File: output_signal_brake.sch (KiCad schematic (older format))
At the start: 35 parts

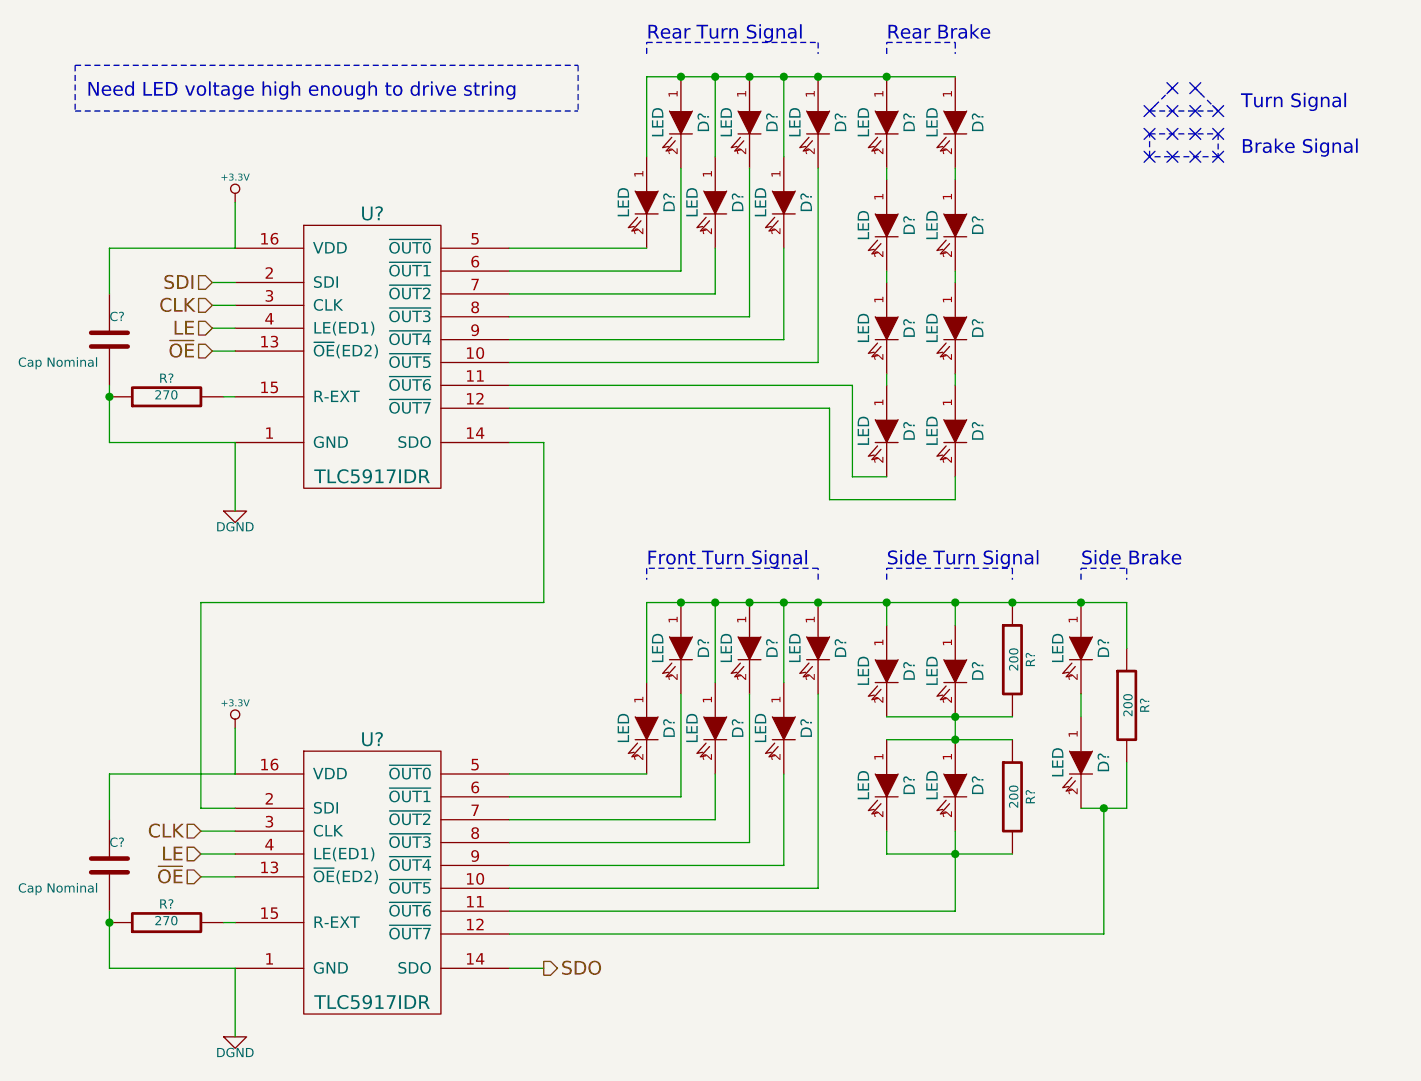
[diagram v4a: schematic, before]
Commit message: revised LED parts to match reality
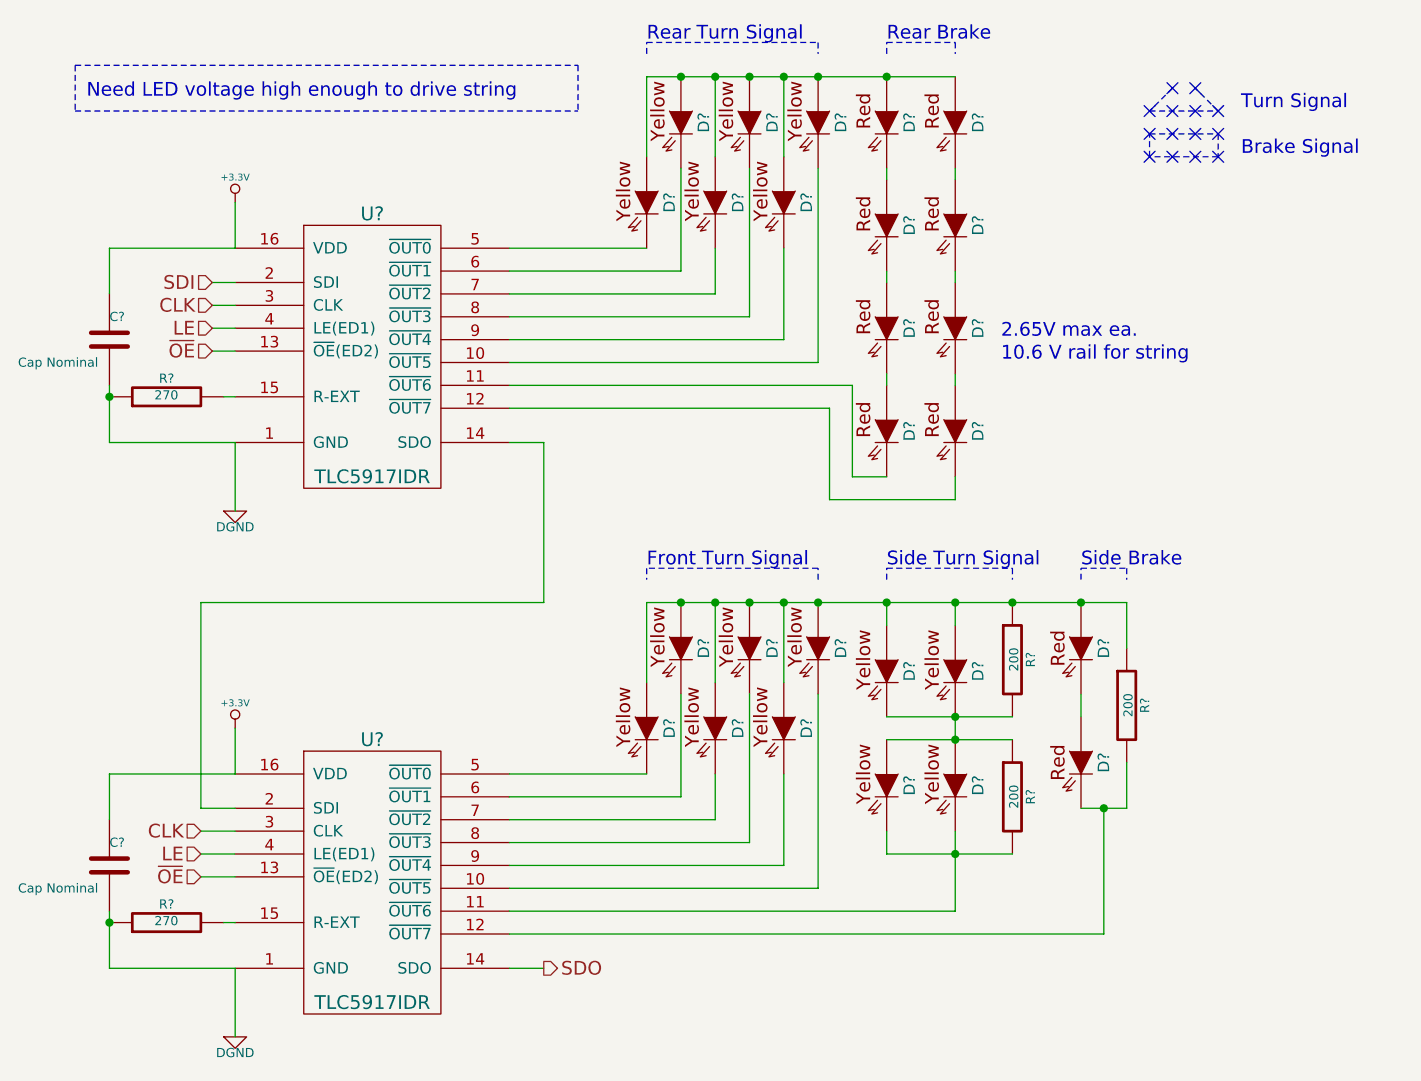
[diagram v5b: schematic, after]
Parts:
- removed D? (x26): LED, ~, symbol LED
- added D? (x8): LS-E63F, ~, symbol LS-E63F
- added D? (x6): LY-E63F, ~, symbol LY-E63F
- added D? (x2): LR-A67F, ~, symbol LR-A67F
- added D? (x10): LY-A67F, ~, symbol LY-A67F
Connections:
- net at U?.10 (~OUT5): now also D?.4 (Cathode)
- net at U?.11 (~OUT6): now also D?.4 (Cathode)
- net at U?.12 (~OUT7): now also D?.4 (Cathode)
- net at U?.5 (~OUT0): now also D?.4 (Cathode)
- net at U?.6 (~OUT1): now also D?.4 (Cathode)
- net at U?.7 (~OUT2): now also D?.4 (Cathode)
- net at U?.8 (~OUT3): now also D?.4 (Cathode)
- net at U?.9 (~OUT4): now also D?.4 (Cathode)
- net at U?.10 (~OUT5): now also D?.2 (Cathode)
- net at R?.2, U?.11 (~OUT6): now also D?.2 (Cathode), D?.2 (Cathode)
- net at R?.2, U?.12 (~OUT7): now also D?.2 (Cathode)
- net at U?.5 (~OUT0): now also D?.2 (Cathode)
- net at U?.6 (~OUT1): now also D?.2 (Cathode)
- net at U?.7 (~OUT2): now also D?.2 (Cathode)
- net at U?.8 (~OUT3): now also D?.2 (Cathode)
- net at U?.9 (~OUT4): now also D?.2 (Cathode)
- net at R?.1, R?.1: now also D?.1 (Anode), D?.1 (Anode), D?.1 (Anode), D?.1 (Anode), D?.1 (Anode), D?.1 (Anode), D?.1 (Anode), D?.1 (Anode), D?.1 (Anode)
- net at R?.1, R?.2: now also D?.1 (Anode), D?.1 (Anode), D?.2 (Cathode), D?.2 (Cathode)
- new net: D?.1 (Anode), D?.1 (Anode), D?.1 (Anode), D?.1 (Anode), D?.1 (Anode), D?.1 (Anode), D?.1 (Anode), D?.1 (Anode)
- new net: D?.1 (Anode), D?.4 (Cathode) (x6)
- new net: D?.1 (Anode), D?.2 (Cathode)
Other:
- note added: "10.6 V rail for string"
- note added: "2.65V max ea."
